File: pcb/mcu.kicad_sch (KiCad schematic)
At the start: 22 parts, among them SW1 GSPTS0018, SW2 GSPTS0018, U1 STM32H730VBTx, Y1 ECS-160-12-33B2Q-JES-TR3

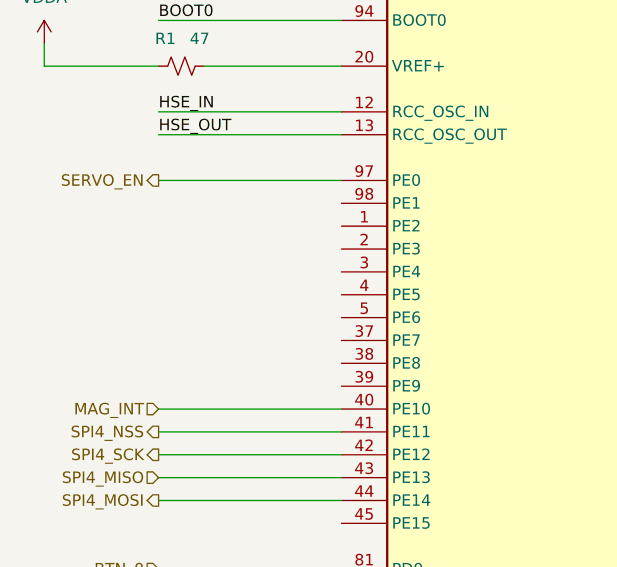
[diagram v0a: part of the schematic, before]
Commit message: Add production files for quoting
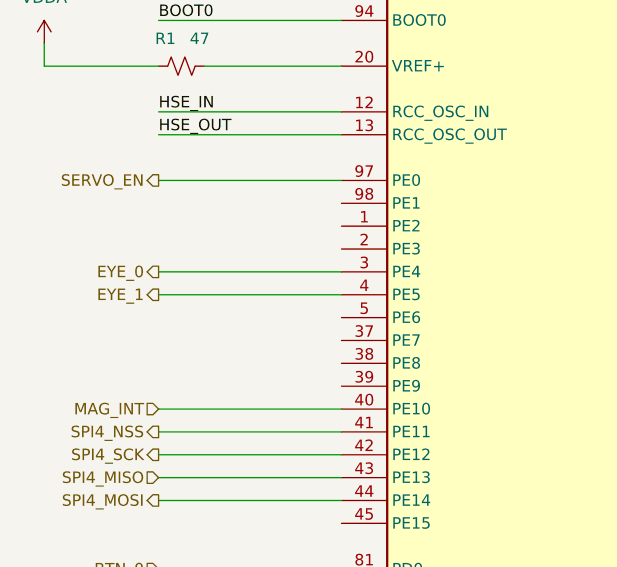
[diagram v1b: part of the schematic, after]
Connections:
- net EYE_0: now reaches U1.3 (PE4)
- net EYE_1: now reaches U1.4 (PE5)

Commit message: Add MPN field for components except resistors
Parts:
- C1, C2: MPN (none) -> GRT188R61H225KE13D
- C10, C11, C13, C14, C15, C5, C7, C8: MPN (none) -> CL10B104KB8NNWC
- C12, C6: MPN (none) -> CL10B105MO8NNWC
- C3: MPN (none) -> GRM188R61E475KE11D
- C4, C9: MPN (none) -> CL10C150JB8NNNC
- FB1: MPN (none) -> BLM18AG601SN1D
- SW1, SW2: MPN (none) -> GSPTS0018
- U1: MPN (none) -> STM32H730VBT6
- Y1: MPN (none) -> ECS-160-12-33B2Q-JES-TR3

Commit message: Update resistor MPNs
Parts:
- R1: MPN (none) -> RC0603JR-1347RL
- R2: MPN (none) -> RC0603FR-0747KL

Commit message: Update MPNs to optimize for HQ Online
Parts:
- C12, C6: MPN CL10B105MO8NNWC -> CL10A105KA8NNNC
- R1: MPN RC0603JR-1347RL -> RC0603FR-0747RL
- SW1, SW2: MPN GSPTS0018 -> SKRPADE010

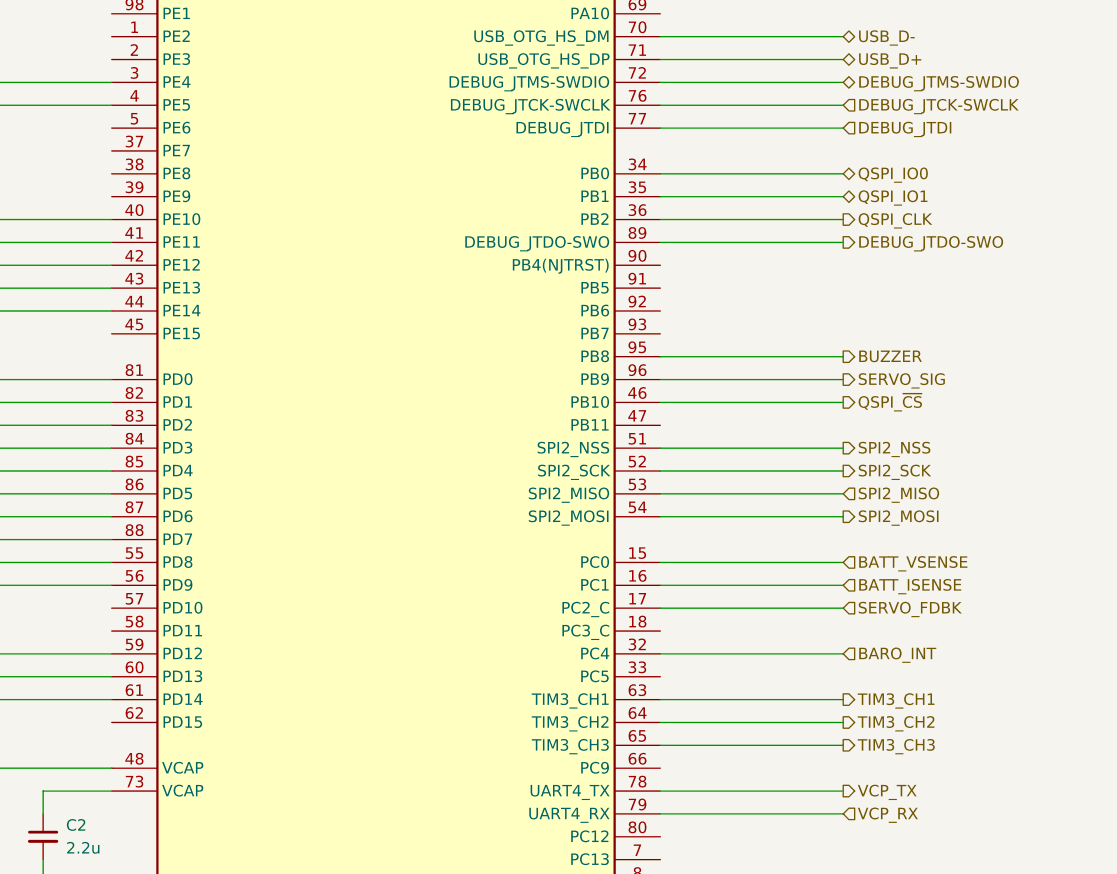
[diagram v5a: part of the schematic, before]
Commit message: Fix QSPI IO0/IO1 swap
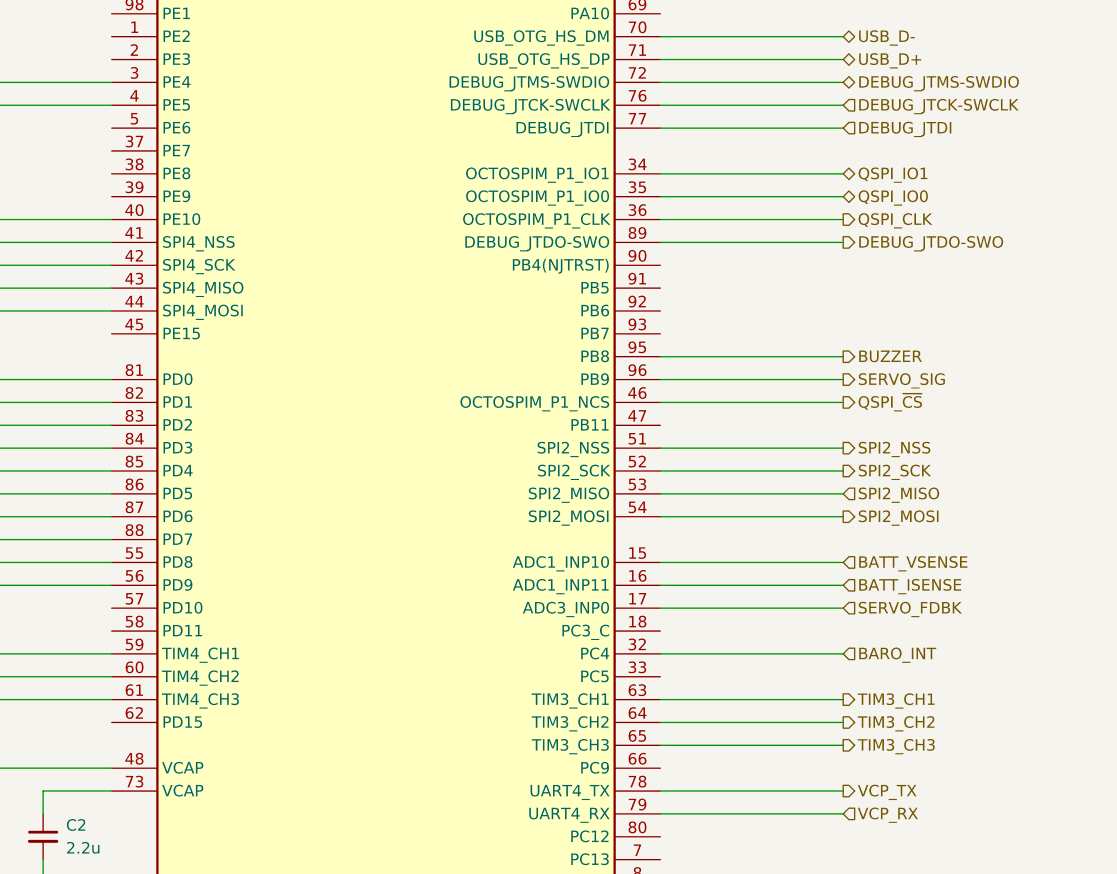
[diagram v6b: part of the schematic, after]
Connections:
- net QSPI_IO0: now also U1.35 (PB1); no longer U1.34 (PB0)
- net QSPI_IO1: now also U1.34 (PB0); no longer U1.35 (PB1)

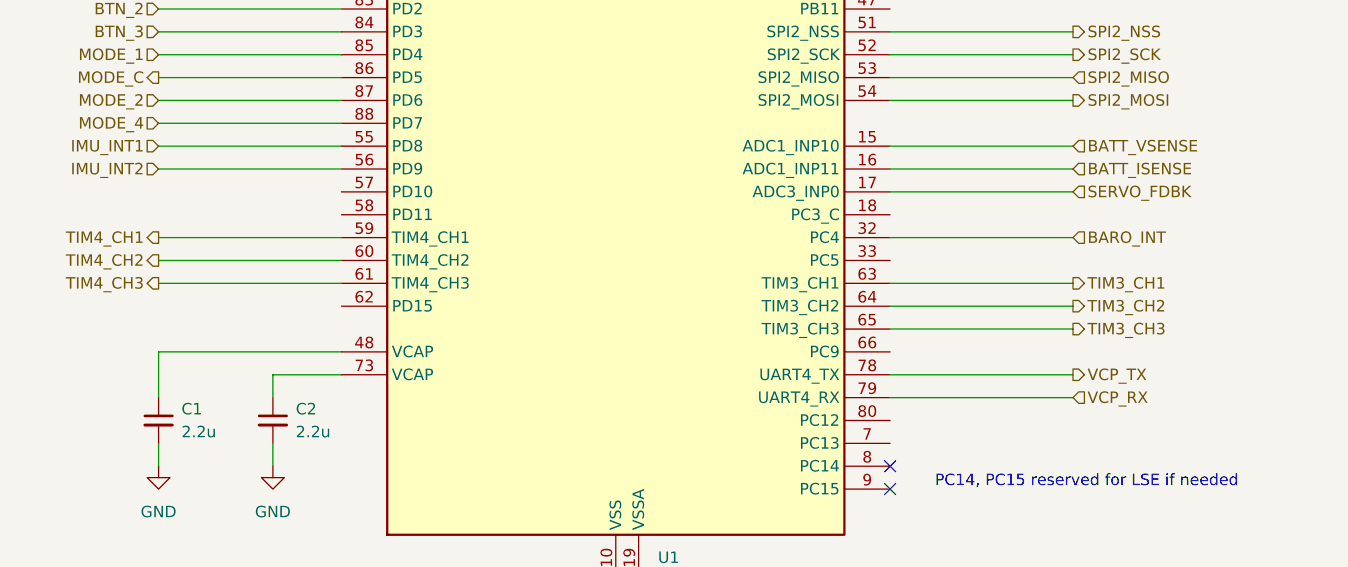
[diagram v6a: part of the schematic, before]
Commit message: Improve baro routing
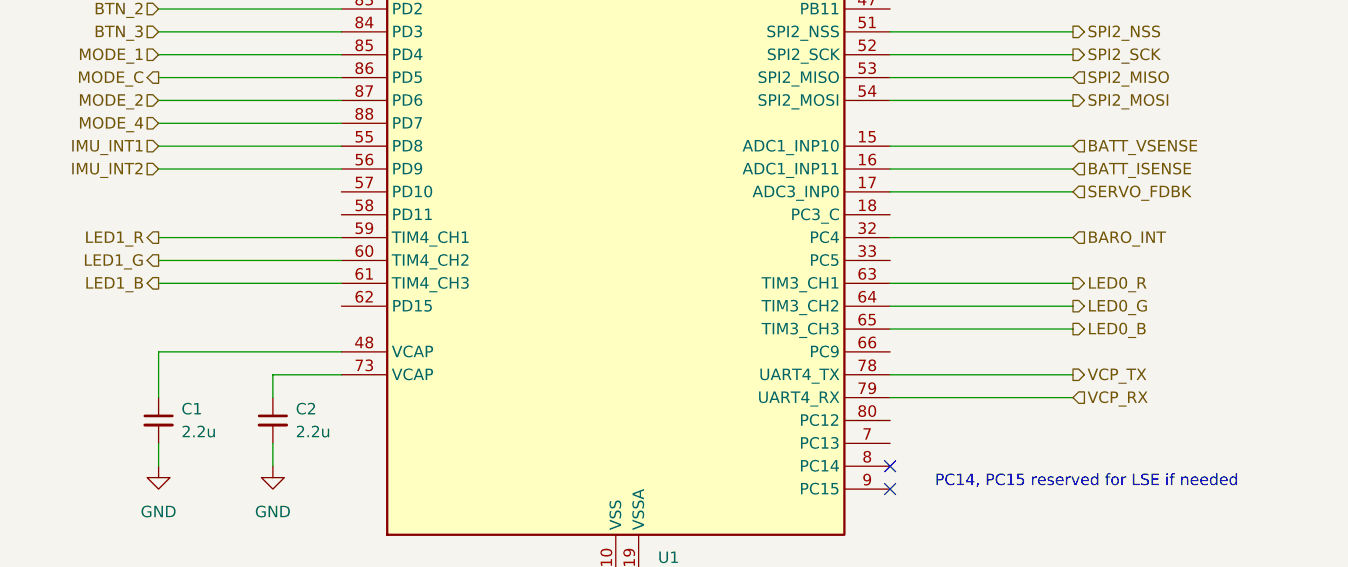
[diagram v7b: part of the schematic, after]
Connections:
- net TIM3_CH1 renamed LED0_R
- net TIM3_CH2 renamed LED0_G
- net TIM3_CH3 renamed LED0_B
- net TIM4_CH1 renamed LED1_R
- net TIM4_CH2 renamed LED1_G
- net TIM4_CH3 renamed LED1_B
